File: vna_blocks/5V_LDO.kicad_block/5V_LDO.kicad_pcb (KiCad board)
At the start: 4 copper layers, 7 parts, among them U11 LT3041ADE-PBF

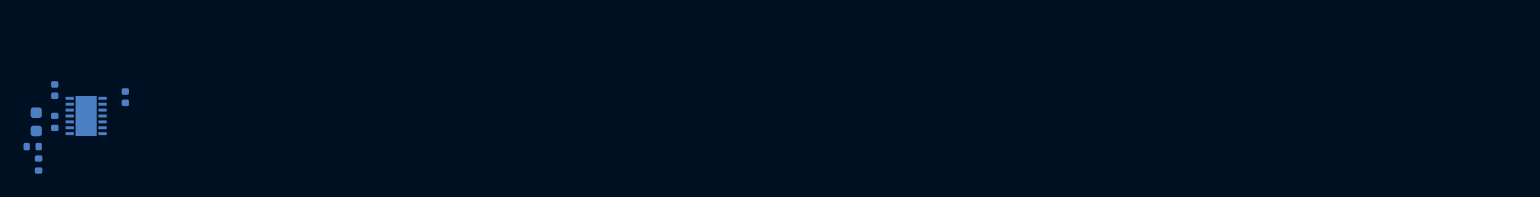
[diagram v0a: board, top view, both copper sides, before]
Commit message: fixed 50 ohm for coax port, fixed power blocks
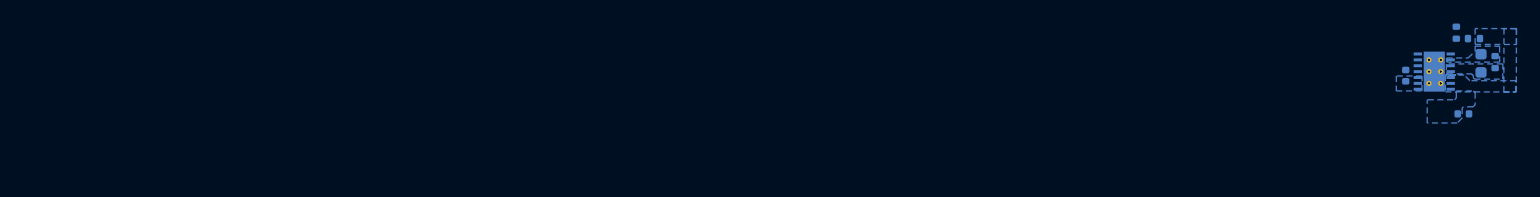
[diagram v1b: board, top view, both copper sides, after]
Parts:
- removed C131, C136: 10u, Capacitor_SMD:C_0402_1005Metric
- removed C134: 4.7u, Capacitor_SMD:C_0603_1608Metric
- removed R44: 49.9k, Resistor_SMD:R_0402_1005Metric
- removed R45: 140k, Resistor_SMD:R_0402_1005Metric
- removed R46: 10k, Resistor_SMD:R_0402_1005Metric
- removed U11: LT3041ADE-PBF, VNA_fp:05-08-1708_ADI-L
- added C138: 10u, Capacitor_SMD:C_0402_1005Metric, B.Cu at (257.8, 112.3)
- added C140: 4.7u, Capacitor_SMD:C_0603_1608Metric, B.Cu at (264.2, 111.2)
- added C141: 10u, Capacitor_SMD:C_0402_1005Metric, B.Cu at (262.7, 115.5)
- added R52: 49.9k, Resistor_SMD:R_0402_1005Metric, B.Cu at (265.4, 111.1)
- added R53: 140k, Resistor_SMD:R_0402_1005Metric, B.Cu at (263.6, 109.1)
- added R54: 10k, Resistor_SMD:R_0402_1005Metric, B.Cu at (262.1, 108.6)
- added U13: LT3041ADE-PBF, VNA_fp:05-08-1708_ADI-L, B.Cu at (260.2, 111.9)
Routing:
- added copper zone on B.Cu, net /5V_RCVR2
- added copper zone on B.Cu, net /Power/5V/+6V_int
- added copper zone on B.Cu, net GNDA
- added copper zone on B.Cu, net Net-(U13-SET)
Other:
- copper layers 4 -> 8
